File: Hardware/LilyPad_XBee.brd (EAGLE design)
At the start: 50 x 50 mm, 39 parts, among them U1 XBEE-1B3, U2 V_REG_LDOSMD

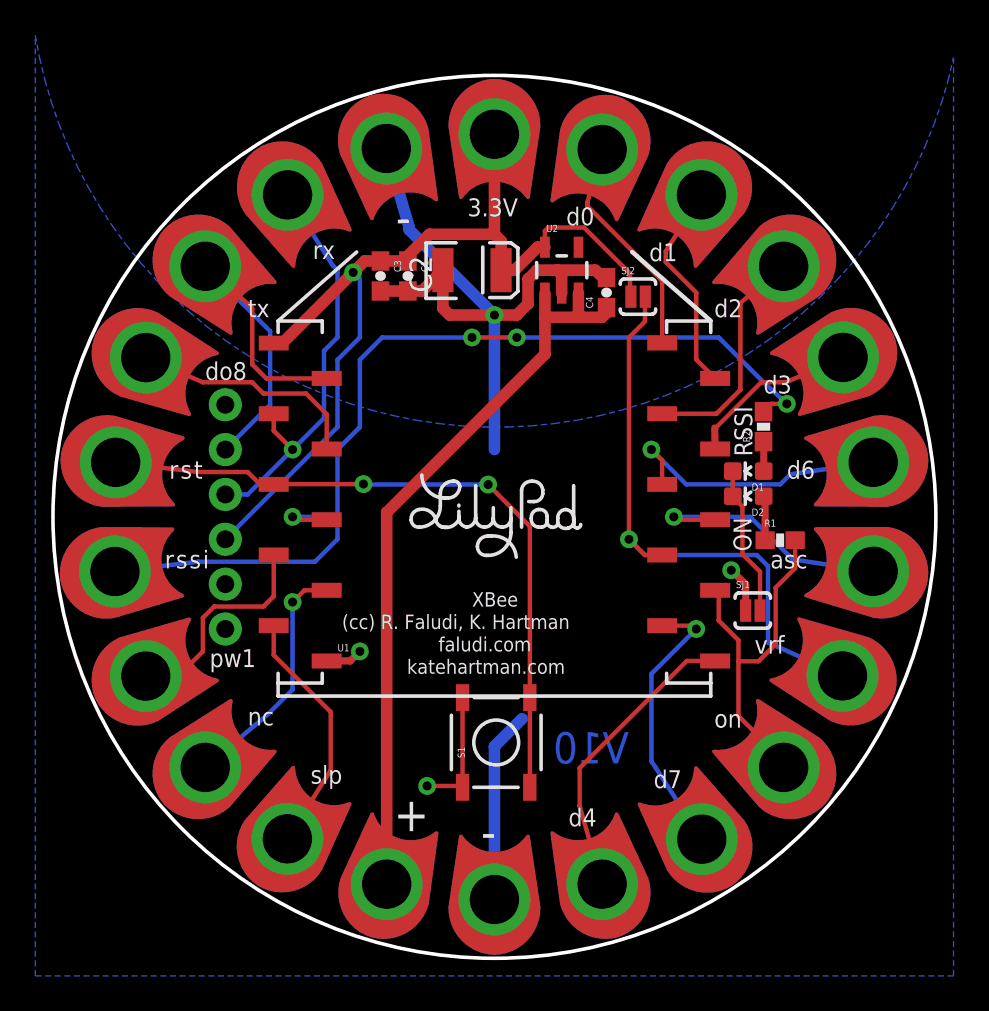
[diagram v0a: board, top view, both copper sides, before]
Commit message: Added Silk / re arranged  LED Resistors
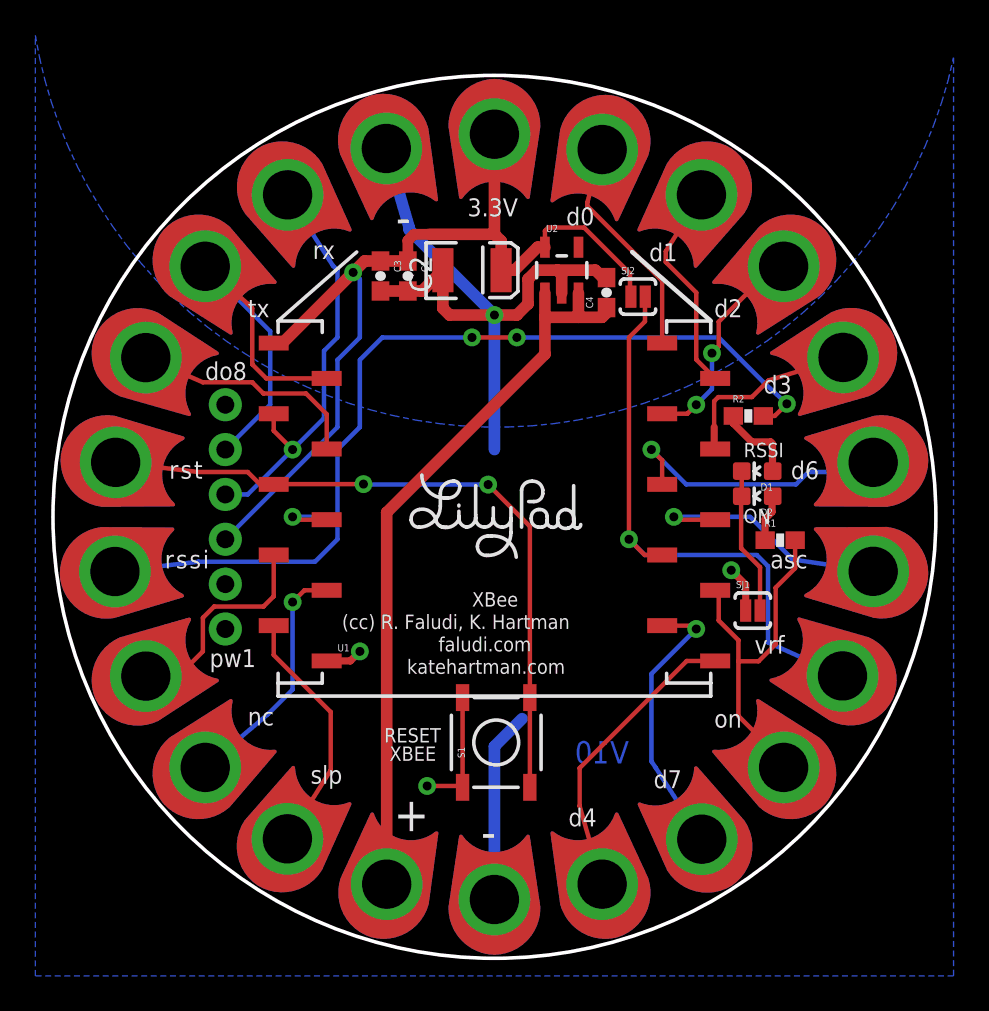
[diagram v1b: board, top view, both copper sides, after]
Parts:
- moved FRAME1 98.6 mm to (-27.2, -36.8)
- moved R2 1.06 mm to (14.4, 5.71), turned to 0 degrees
- moved D1 0.51 mm to (14.9, 2.59)
- moved D2 0.51 mm to (14.9, 1.17)
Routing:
- net N$1: track 1.67 -> 4.67 mm
- net D3: track 9.83 -> 10.7 mm
- net N$3: track 9.21 -> 8.36 mm
- net D2: track 13.1 -> 12.3 mm, vias 0 -> 2
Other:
- board text added: "RESET"
- board text added: "XBEE"

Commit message: Added Copper Flame/ Silk for jumper
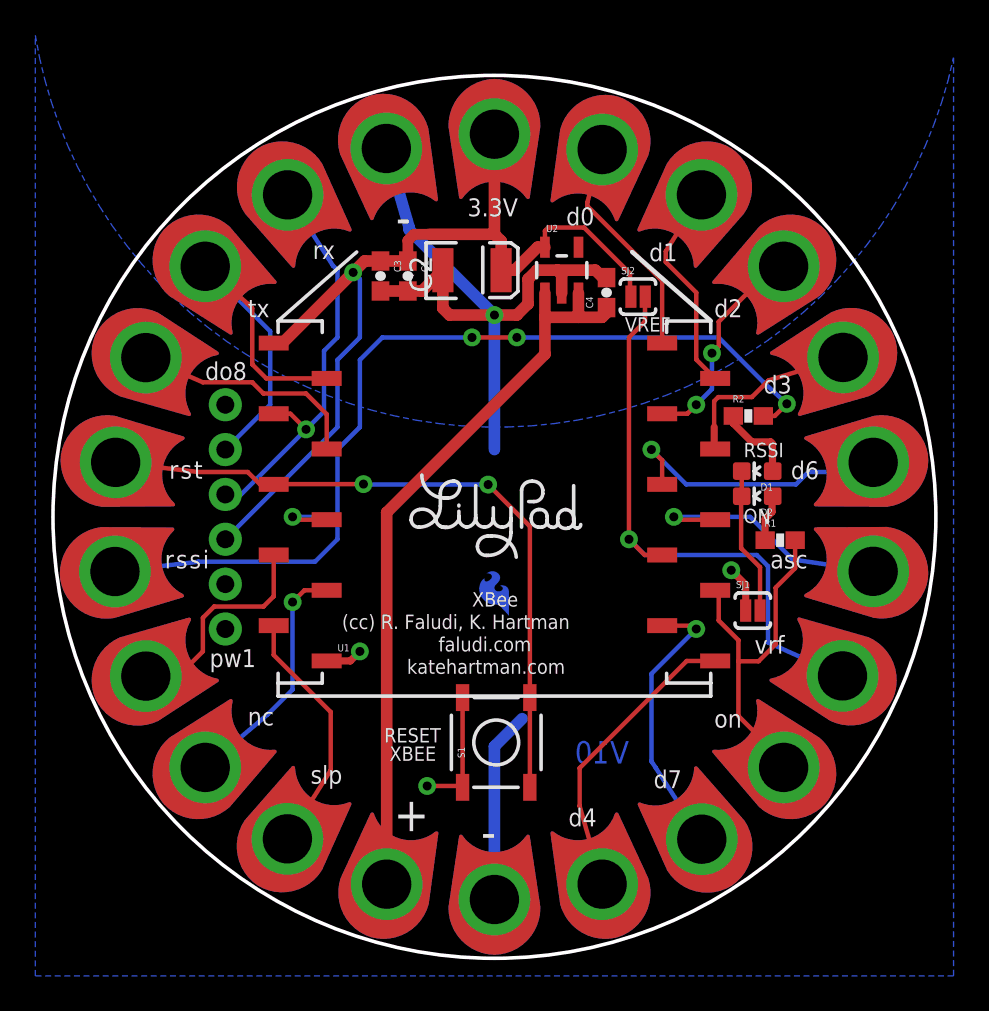
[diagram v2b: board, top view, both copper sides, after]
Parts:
- added LOGO1: SFE_LOGO_FLAME.1COP, SparkFun-Aesthetics:SFE_LOGO_FLAME_COPPER_.1
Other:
- board text added: "VREF"
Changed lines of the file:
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@@
 <text x="-8.636" y="-6.35" size="0.8128" layer="21" font="vector" ratio="15">(cc) R. Faludi, K. Hartman</text>
 <text x="-3.175" y="-7.62" size="0.8128" layer="21" font="vector" ratio="15">faludi.com</text>
-<text x="-16.891" y="3.302" size="1.016" layer="22" font="vector" ratio="15" rot="MR0">TXO</text>
-<text x="-16.891" y="0.762" size="1.016" layer="22" font="vector" ratio="15" rot="MR0">RXI</text>
-<text x="-16.891" y="-1.778" size="1.016" layer="22" font="vector" ratio="15" rot="MR0">3.3V</text>
-<text x="-16.891" y="-6.858" size="1.016" layer="22" font="vector" ratio="15" rot="MR0">GND</text>
+<text x="-11.176" y="3.429" size="1.016" layer="22" font="vector" ratio="15" rot="MR0">TXO</text>
+<text x="-11.43" y="0.889" size="1.016" layer="22" font="vector" ratio="15" rot="MR0">RXI</text>
+<text x="-10.668" y="-1.905" size="1.016" layer="22" font="vector" ratio="15" rot="MR0">3.3V</text>
+<text x="-11.049" y="-6.858" size="1.016" layer="22" font="vector" ratio="15" rot="MR0">GND</text>
 <text x="-16.383" y="7.239" size="1.016" layer="22" font="vector" ratio="15" rot="MR0">4</text>
 <text x="-12.954" y="11.303" size="1.016" layer="22" font="vector" ratio="15" rot="MR0">2</text>
@@
 <text x="-6.2484" y="-12.7762" size="0.8128" layer="21" font="vector" ratio="15">RESET </text>
 <text x="-5.9436" y="-13.8176" size="0.8128" layer="21" font="vector" ratio="15">XBEE</text>
+<text x="9.9822" y="11.303" size="0.8128" layer="21" font="vector" ratio="15" rot="R180">VREF</text>
 </plain>
 <attributes>
@@
 <element name="U$2" library="SparkFun-Aesthetics" package="OSHW-LOGO-L" value="" x="0" y="1.016" rot="MR0"/>
 <element name="FRAME1" library="SparkFun-Aesthetics" package="CREATIVE_COMMONS" value="FRAME-LETTER" x="-27.159478125" y="-36.83"/>
+<element name="LOGO1" library="SparkFun-Aesthetics" package="SFE_LOGO_FLAME_COPPER_.1" value="SFE_LOGO_FLAME.1COP" x="1.143" y="-5.969" rot="MR0"/>
 </elements>
 <signals>
@@
 <contactref element="S1" pad="1"/>
 <contactref element="S1" pad="2"/>
-<wire x1="-1.8034" y1="-10.2362" x2="-1.8034" y2="-15.3162" width="0.254" layer="1"/>
 <via x="-3.81" y="-15.24" extent="1-16" drill="0.508"/>
-<wire x1="-1.8034" y1="-15.3162" x2="-1.8796" y2="-15.24" width="0.254" layer="1"/>
-<wire x1="-1.8796" y1="-15.24" x2="-3.81" y2="-15.24" width="0.254" layer="1"/>
 <wire x1="14.2295" y1="-5.3086" x2="14.2295" y2="-3.8409" width="0.4064" layer="1"/>
 <wire x1="14.2295" y1="-3.8409" x2="13.4112" y2="-3.0226" width="0.4064" layer="1"/>
+<wire x1="-3.81" y1="-15.24" x2="-1.8796" y2="-15.24" width="0.254" layer="1"/>
+<wire x1="-1.8796" y1="-15.24" x2="-1.8034" y2="-15.3162" width="0.254" layer="1"/>
+<wire x1="-1.8034" y1="-10.2362" x2="-1.8034" y2="-15.3162" width="0.254" layer="1"/>
 </signal>
 <signal name="VCC" class="1">
@@
 <contactref element="U1" pad="3"/>
 <contactref element="U$45" pad="1"/>
-<wire x1="-9.652" y1="9.398" x2="-9.652" y2="7.188" width="0.254" layer="16"/>
 <wire x1="-9.652" y1="9.398" x2="-8.89" y2="10.16" width="0.254" layer="16"/>
 <wire x1="-9.144" y1="14.224" x2="-11.713790625" y2="18.234753125" width="0.254" layer="16"/>
 <wire x1="-8.89" y1="13.97" x2="-9.144" y2="14.224" width="0.254" layer="16"/>
 <wire x1="-8.89" y1="10.16" x2="-8.89" y2="13.97" width="0.254" layer="16"/>
-<wire x1="-13.97" y1="1.27" x2="-15.24" y2="1.27" width="0.254" layer="16"/>
-<wire x1="-9.652" y1="7.188" x2="-9.652" y2="5.588" width="0.254" layer="16"/>
-<wire x1="-9.652" y1="5.588" x2="-11.43" y2="3.81" width="0.254" layer="16"/>
-<wire x1="-11.43" y1="3.81" x2="-13.97" y2="1.27" width="0.254" layer="16"/>
-<wire x1="-12.5" y1="4.88" x2="-12.5" y2="5.84" width="0.254" layer="1"/>
-<wire x1="-11.43" y1="3.81" x2="-12.5" y2="4.88" width="0.254" layer="1"/>
-<via x="-11.43" y="3.81" extent="1-16" drill="0.508"/>
+<via x="-10.668" y="4.953" extent="1-16" drill="0.508"/>
+<wire x1="-9.652" y1="9.398" x2="-9.652" y2="5.969" width="0.254" layer="16"/>
+<wire x1="-9.652" y1="5.969" x2="-10.668" y2="4.953" width="0.254" layer="16"/>
+<wire x1="-12.5" y1="5.84" x2="-11.555" y2="5.84" width="0.254" layer="1"/>
+<wire x1="-11.555" y1="5.84" x2="-10.668" y2="4.953" width="0.254" layer="1"/>
+<wire x1="-15.24" y1="1.27" x2="-14.351" y2="1.27" width="0.254" layer="16"/>
+<wire x1="-14.351" y1="1.27" x2="-10.668" y2="4.953" width="0.254" layer="16"/>
 </signal>
 <signal name="TX-O">
